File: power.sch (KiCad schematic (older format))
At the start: 3 parts

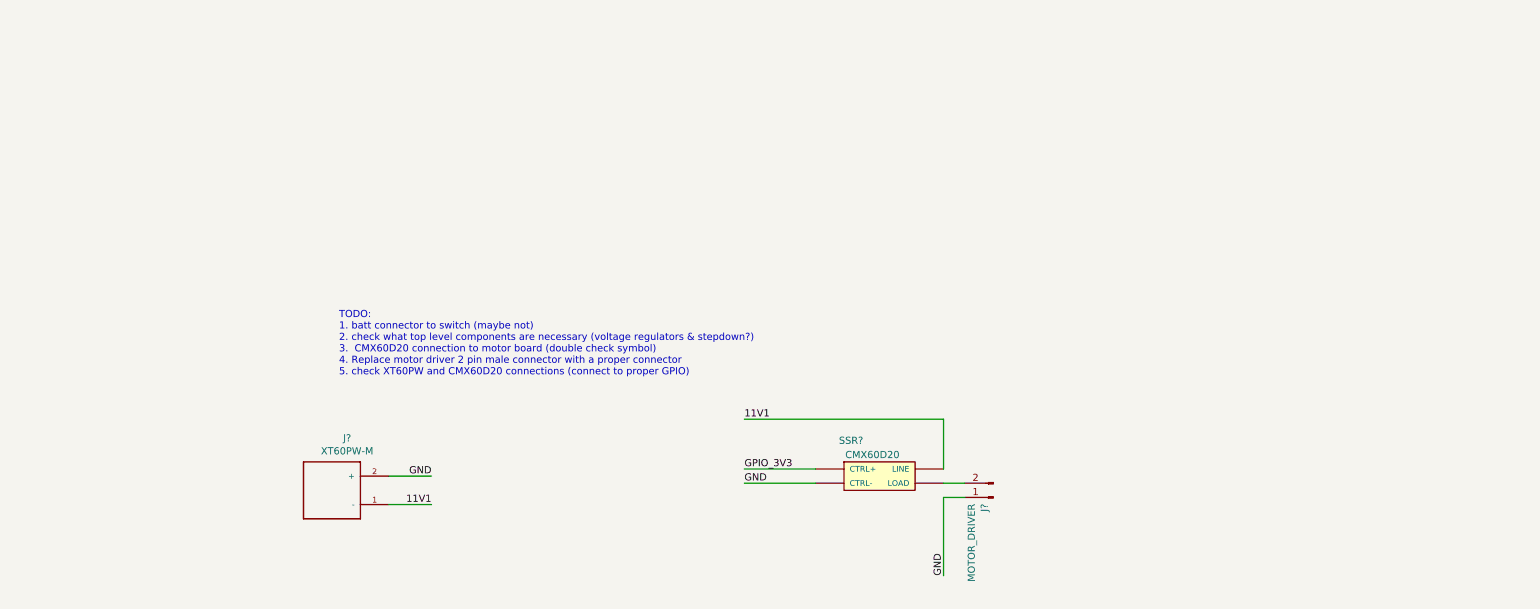
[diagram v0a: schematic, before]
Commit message: fixed XT60PW-M symbol
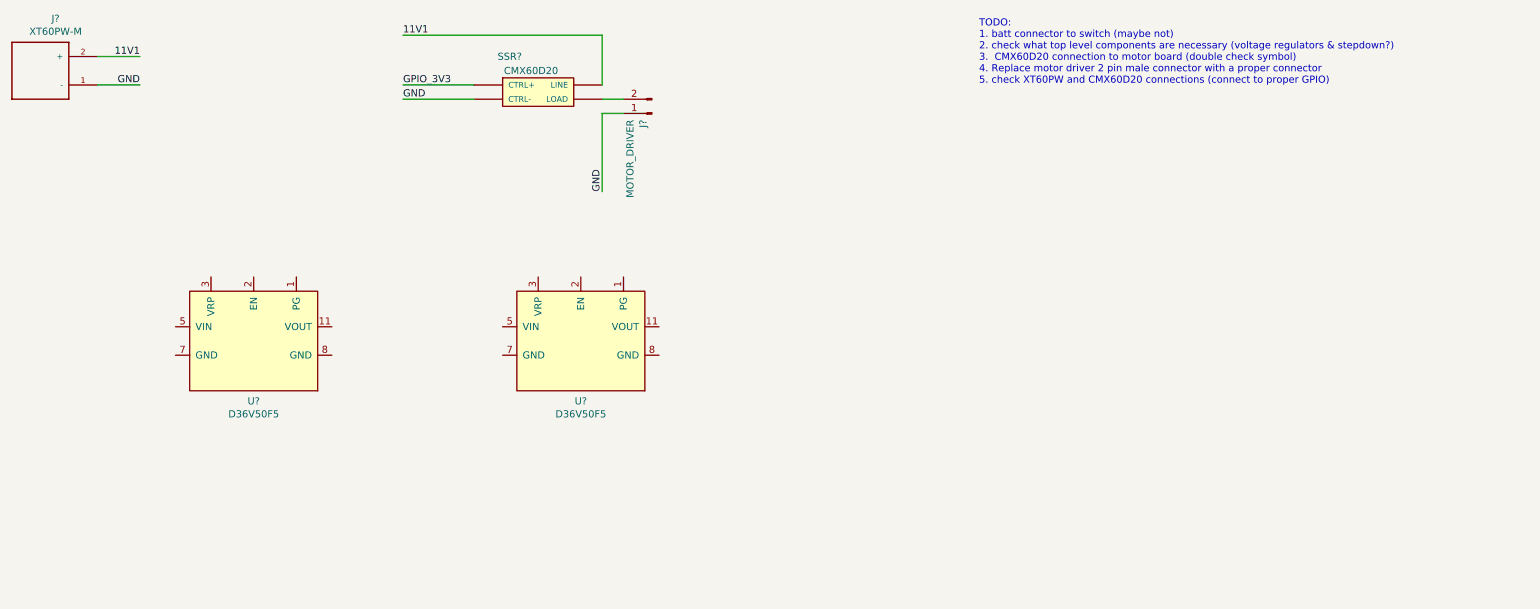
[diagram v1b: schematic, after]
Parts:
- added U? (x2): D36V50F5, Drone:D36V50F5, symbol Drone:D36V50F5
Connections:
- net 11V1: now also J?.2 (+); no longer J?.1 (-)
- net GND: now also J?.1 (-); no longer J?.2 (+)
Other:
- moved on the sheet: J?, SSR?
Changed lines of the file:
@@
 $Descr A4 11693 8268
 encoding utf-8
-Sheet 5 5
+Sheet 4 5
 Title ""
 Date ""
@@
 Comment4 ""
 $EndDescr
-Text Notes 3250 3250 0    50   ~ 0
+Text Notes 7750 1200 0    50   ~ 0
 TODO: \n1. batt connector to switch (maybe not)\n2. check what top level components are necessary (voltage regulators & stepdown?)\n3.  CMX60D20 connection to motor board (double check symbol)\n4. Replace motor driver 2 pin male connector with a proper connector\n5. check XT60PW and CMX60D20 connections (connect to proper GPIO)
 $Comp
 L Drone:CMX60D20 SSR?
 U 1 1 5E3F8AD0
-P 7050 3850
+P 4650 1150
 AR Path="/5E3F8AD0" Ref="SSR?"  Part="1"
 AR Path="/5E3E92F4/5E3F8AD0" Ref="U?"  Part="1"
-F 0 "U?" H 6850 4000 50  0000 C CNN
-F 1 "CMX60D20" H 7000 3900 50  0000 C CNN
-F 2 "Drone:CMX60D20" H 6950 3850 50  0001 L BNN
-F 3 "https://www.tme.com/Document/b27c1a9b330ca081d5500ebe72e3b05d/c_m_x.pdf" H 7050 3850 50  0001 C CNN
-	1    7050 3850
+F 0 "U?" H 4450 1300 50  0000 C CNN
+F 1 "CMX60D20" H 4600 1200 50  0000 C CNN
+F 2 "Drone:CMX60D20" H 4550 1150 50  0001 L BNN
+F 3 "https://www.tme.com/Document/b27c1a9b330ca081d5500ebe72e3b05d/c_m_x.pdf" H 4650 1150 50  0001 C CNN
+	1    4650 1150
 	1    0    0    -1
 $EndComp
-Text Label 6100 4000 0    50   ~ 0
+Text Label 3700 1300 0    50   ~ 0
 GND
 Wire Wire Line
-	6100 4000 6600 4000
-Text Label 6100 3900 0    50   ~ 0
+	3700 1300 4200 1300
+Text Label 3700 1200 0    50   ~ 0
 GPIO_3V3
-Text Label 6100 3550 0    50   ~ 0
+Text Label 3700 850  0    50   ~ 0
 11V1
 $Comp
 L Connector:Conn_01x02_Male J?
 U 1 1 5E3F8ADC
-P 7850 4100
-F 0 "J?" V 7912 4144 50  0000 L CNN
-F 1 "MOTOR_DRIVER" V 8003 4144 50  0000 L CNN
-F 2 "" H 7850 4100 50  0001 C CNN
-F 3 "~" H 7850 4100 50  0001 C CNN
-	1    7850 4100
+P 5450 1400
+F 0 "J?" V 5512 1444 50  0000 L CNN
+F 1 "MOTOR_DRIVER" V 5603 1444 50  0000 L CNN
+F 2 "" H 5450 1400 50  0001 C CNN
+F 3 "~" H 5450 1400 50  0001 C CNN
+	1    5450 1400
 	-1   0    0    1
 $EndComp
-Text Label 7500 4650 1    50   ~ 0
+Text Label 5100 1950 1    50   ~ 0
 GND
 $Comp
 L Drone:XT60PW-M J?
 U 1 1 5E3FF515
-P 3200 4050
-F 0 "J?" H 3093 3683 50  0000 C CNN
-F 1 "XT60PW-M" H 3093 3774 50  0000 C CNN
-F 2 "Drone:XT60PW-M" H 3150 4350 50  0001 L BNN
-F 3 "https://www.snapeda.com/parts/XT60PW-M%20/AMASS/datasheet/" H 3150 4150 50  0001 L BNN
-	1    3200 4050
+P 1150 1100
+AR Path="/5E3FF515" Ref="J?"  Part="1"
+AR Path="/5E3E92F4/5E3FF515" Ref="J?"  Part="1"
+F 0 "J?" H 1043 733 50  0000 C CNN
+F 1 "XT60PW-M" H 1043 824 50  0000 C CNN
+F 2 "Drone:XT60PW-M" H 1100 1400 50  0001 L BNN
+F 3 "https://www.snapeda.com/parts/XT60PW-M%20/AMASS/datasheet/" H 1100 1200 50  0001 L BNN
+	1    1150 1100
 	-1   0    0    1
 $EndComp
-Text Label 3900 4150 2    50   ~ 0
+Text Label 1850 1000 2    50   ~ 0
 11V1
 Wire Wire Line
-	3900 4150 3600 4150
-Text Label 3900 3950 2    50   ~ 0
+	1850 1200 1550 1200
+Text Label 1850 1200 2    50   ~ 0
 GND
 Wire Wire Line
-	3900 3950 3600 3950
+	1850 1000 1550 1000
 Wire Wire Line
-	6600 3900 6100 3900
+	4200 1200 3700 1200
 Wire Wire Line
-	7500 3550 7500 3900
+	5100 850  5100 1200
 Wire Wire Line
-	6100 3550 7500 3550
+	3700 850  5100 850
 Wire Wire Line
-	7500 4000 7650 4000
+	5100 1300 5250 1300
 Wire Wire Line
-	7650 4100 7500 4100
+	5250 1400 5100 1400
 Wire Wire Line
-	7500 4100 7500 4650
+	5100 1400 5100 1950
+$Comp
+L Drone:D36V50F5 U?
+U 1 1 5E3ABE9B
+P 2650 3000
+F 0 "U?" H 2650 2577 50  0000 C CNN
+F 1 "D36V50F5" H 2650 2486 50  0000 C CNN
+F 2 "Drone:D36V50F5" H 2600 2950 50  0001 C CNN
+F 3 "https://www.pololu.com/product/4091" H 2600 2950 50  0001 C CNN
+	1    2650 3000
+	1    0    0    -1
+$EndComp
+$Comp
+L Drone:D36V50F5 U?
+U 1 1 5E3AC357
+P 4950 3000
+F 0 "U?" H 4950 2577 50  0000 C CNN
+F 1 "D36V50F5" H 4950 2486 50  0000 C CNN
+F 2 "Drone:D36V50F5" H 4900 2950 50  0001 C CNN
+F 3 "https://www.pololu.com/product/4091" H 4900 2950 50  0001 C CNN
+	1    4950 3000
+	1    0    0    -1
+$EndComp
 $EndSCHEMATC
